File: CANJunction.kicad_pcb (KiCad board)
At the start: 2 copper layers, 46.3 x 22.6 mm, 7 parts, among them J1 Screw_Terminal_01x02, J2 Screw_Terminal_01x06, J3 Screw_Terminal_01x02

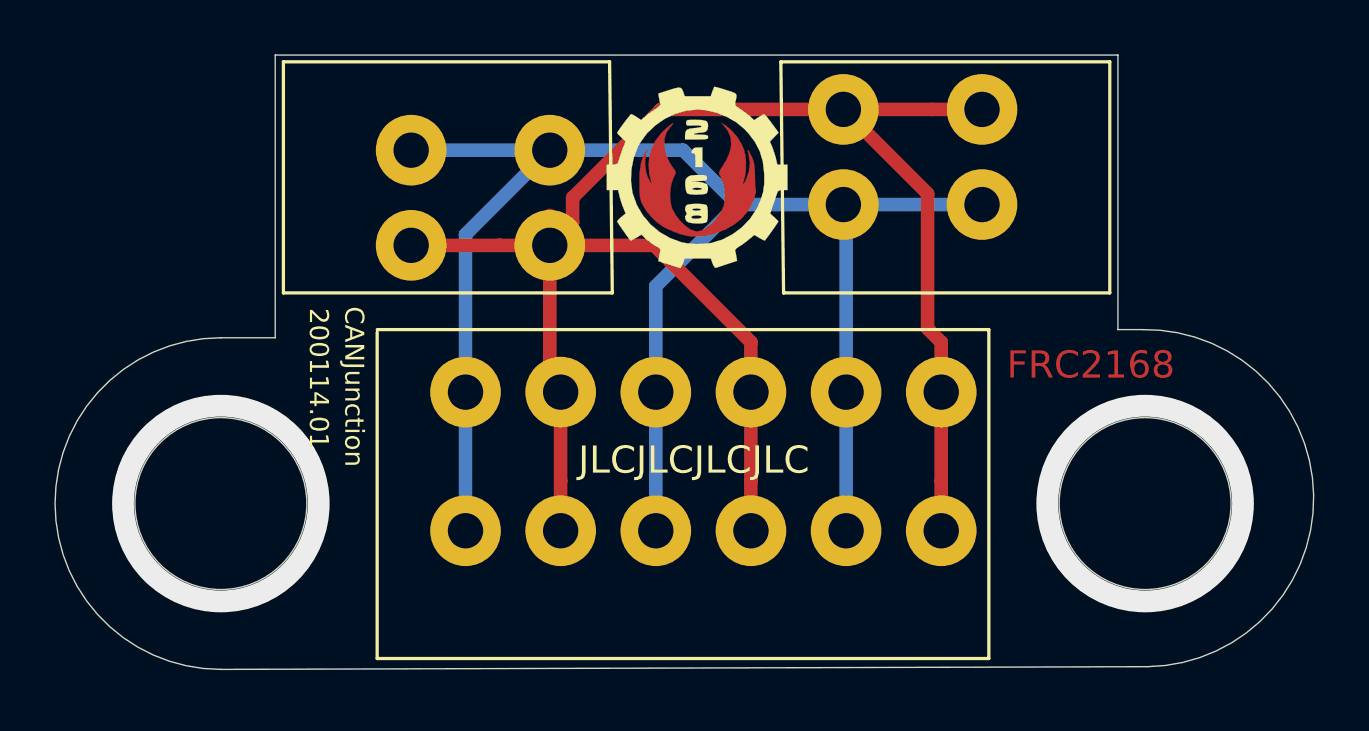
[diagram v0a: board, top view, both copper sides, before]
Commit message: update layout mod hole to fit  3/16” rivet or “10 bolt
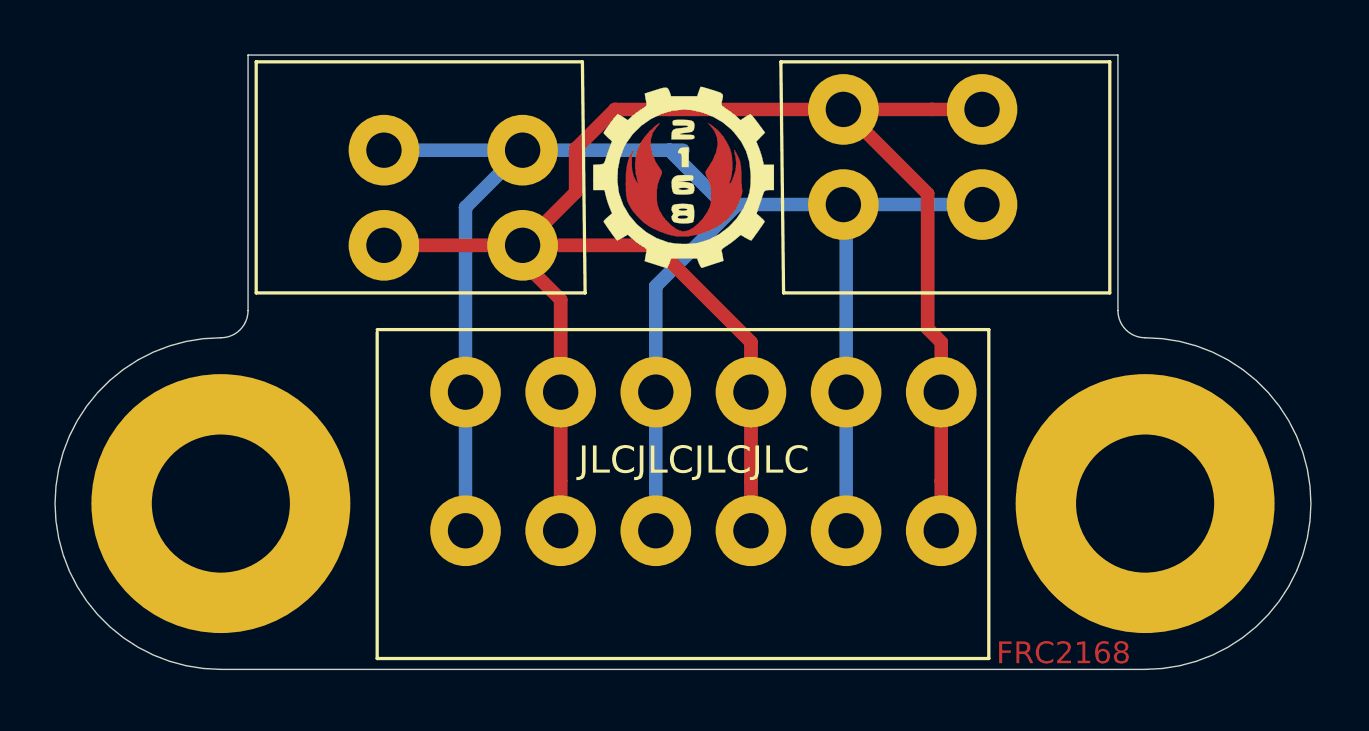
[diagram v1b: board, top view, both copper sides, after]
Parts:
- added H1: MountingHole, _canjunction:mounting_holes, F.Cu at (126.0, 66.0)
- moved J1 1.00 mm to (132.0, 53.0)
- moved G*** 0.50 mm to (143.0, 54.0) (x2)
- moved Wings 0.50 mm to (143.0, 54.0) (x2)
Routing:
- net Net-(J1-Pad2): track 68.2 -> 71.3 mm
- net (no net): vias 2 -> 0
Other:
- board size 46.3 x 22.6 mm -> 46.2 x 22.6 mm
- rule pad_to_mask_clearance: 0.051 -> 0
- board text added: "211209.01"
- board text removed: "200114.01"

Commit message: add direction to fab on where to place order number
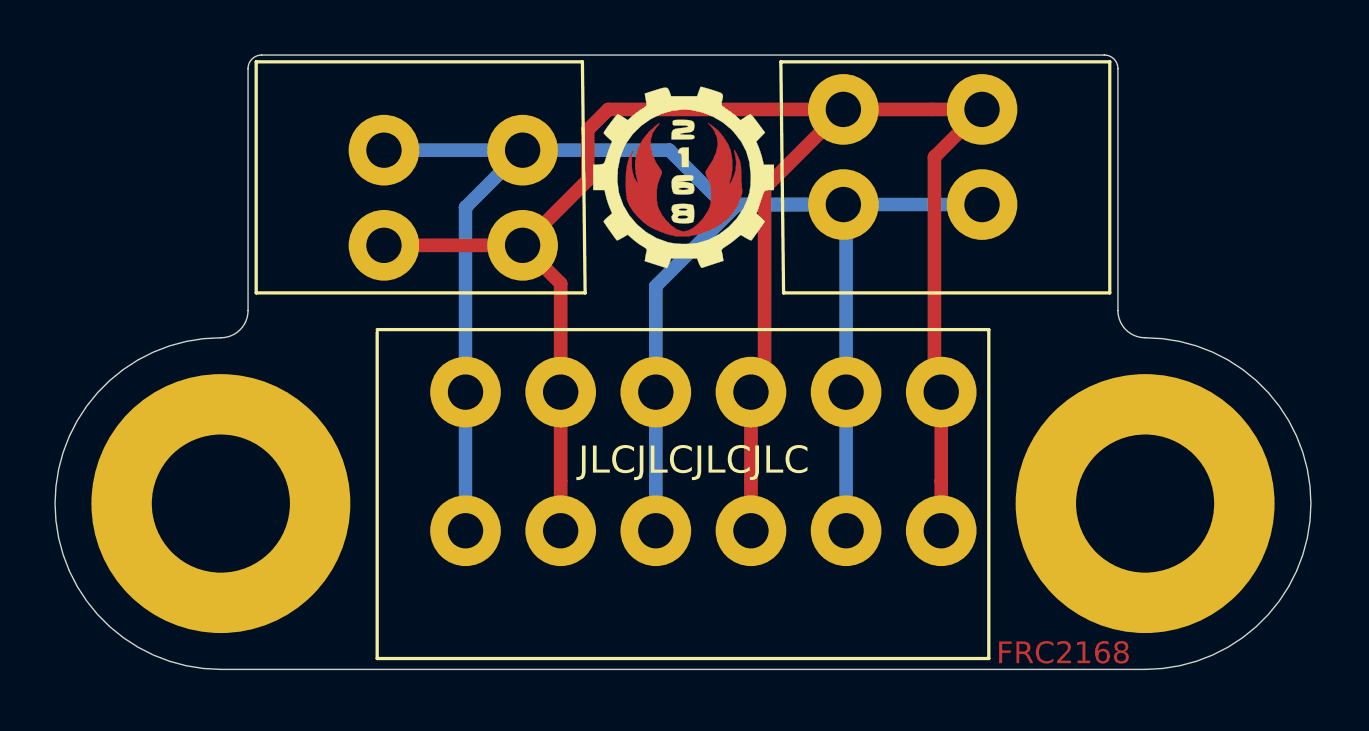
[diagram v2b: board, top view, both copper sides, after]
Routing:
- net Net-(J1-Pad1): track 62.0 -> 66.9 mm
- net Net-(J1-Pad2): track 71.3 -> 70.0 mm
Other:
- outline, holes or cut-outs redrawn
- board text added: "Place Order Number in place of text "JLCJLCJLCJLC" on F.Silk layer"
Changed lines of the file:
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@@
   (general
     (thickness 1.6)
-    (drawings 15)
-    (tracks 40)
+    (drawings 22)
+    (tracks 37)
     (zones 0)
     (modules 8)
@@
     (38 B.Mask user)
     (39 F.Mask user)
-    (40 Dwgs.User user)
-    (41 Cmts.User user)
+    (40 Dwgs.User user hide)
+    (41 Cmts.User user hide)
     (42 Eco1.User user)
     (43 Eco2.User user)
     (44 Edge.Cuts user)
     (45 Margin user)
-    (46 B.CrtYd user)
-    (47 F.CrtYd user)
-    (48 B.Fab user)
+    (46 B.CrtYd user hide)
+    (47 F.CrtYd user hide)
+    (48 B.Fab user hide)
     (49 F.Fab user)
   )
@@
     (pad_to_mask_clearance 0)
     (aux_axis_origin 0 0)
-    (visible_elements 7FFFFFFF)
+    (visible_elements 7FFFFF9F)
     (pcbplotparams
-      (layerselection 0x010fc_ffffffff)
+      (layerselection 0x012fc_ffffffff)
       (usegerberextensions false)
       (usegerberattributes false)
@@
       (effects (font (size 1 1) (thickness 0.15)))
     )
-    (fp_text value MountingHole (at 0 -0.5) (layer F.Fab)
+    (fp_text value MountingHole (at 0 -0.5) (layer F.Fab) hide
       (effects (font (size 1 1) (thickness 0.15)))
     )
@@
     )
   )
+  (gr_line (start 143.75 65.25) (end 143.75 74.75) (layer F.Fab) (width 0.15))
+  (gr_line (start 143 66.5) (end 144.5 66.5) (layer F.Fab) (width 0.15))
+  (gr_line (start 144.5 66.5) (end 143.75 65.25) (layer F.Fab) (width 0.15))
+  (gr_line (start 143.75 65.25) (end 143 66.5) (layer F.Fab) (width 0.15))
+  (gr_text "Place Order Number in place of\ntext \"JLCJLCJLCJLC\" on F.Silk layer" (at 143.75 76.75) (layer F.Fab)
+    (effects (font (size 1 1) (thickness 0.15)))
+  )
+  (gr_arc (start 158.5 50) (end 159 50) (angle -90) (layer Edge.Cuts) (width 0.05))
+  (gr_arc (start 127.5 50) (end 127.5 49.5) (angle -90) (layer Edge.Cuts) (width 0.05))
   (gr_arc (start 126 58.9) (end 126 59.9) (angle -90) (layer Edge.Cuts) (width 0.05))
   (gr_line (start 126 72.1) (end 160 72.1) (layer Edge.Cuts) (width 0.05))
@@
     (effects (font (size 1 1) (thickness 0.15)) (justify mirror))
   )
-  (gr_line (start 127 58.9) (end 127 49.5) (layer Edge.Cuts) (width 0.05))
-  (gr_line (start 159 49.5) (end 159 58.9) (layer Edge.Cuts) (width 0.05))
-  (gr_line (start 127 49.5) (end 159 49.5) (layer Edge.Cuts) (width 0.05))
+  (gr_line (start 127 58.9) (end 127 50) (layer Edge.Cuts) (width 0.05))
+  (gr_line (start 159 50) (end 159 58.9) (layer Edge.Cuts) (width 0.05))
+  (gr_line (start 127.5 49.5) (end 158.5 49.5) (layer Edge.Cuts) (width 0.05))
   (segment (start 148.9 55) (end 145 55) (width 0.5) (layer B.Cu) (net 1))
-  (segment (start 138.1 53) (end 143 53) (width 0.5) (layer B.Cu) (net 1))
-  (segment (start 142.5 53) (end 144.5 55) (width 0.5) (layer B.Cu) (net 1))
   (segment (start 154 55) (end 148.9 55) (width 0.5) (layer B.Cu) (net 1))
   (segment (start 135 61.9) (end 135 67) (width 0.5) (layer B.Cu) (net 1))
@@
   (segment (start 137.1 53) (end 135 55.1) (width 0.5) (layer B.Cu) (net 1))
   (segment (start 137.1 53) (end 132 53) (width 0.5) (layer B.Cu) (net 1))
+  (segment (start 142.5 53) (end 137.1 53) (width 0.5) (layer B.Cu) (net 1))
+  (segment (start 144.5 55) (end 142.5 53) (width 0.5) (layer B.Cu) (net 1))
+  (segment (start 148.9 55) (end 144.5 55) (width 0.5) (layer B.Cu) (net 1))
   (segment (start 152.161523 51.5) (end 148.9 51.5) (width 0.5) (layer F.Cu) (net 2))
   (segment (start 154 51.5) (end 152.161523 51.5) (width 0.5) (layer F.Cu) (net 2))
-  (segment (start 138.1 56.5) (end 136.261523 56.5) (width 0.5) (layer F.Cu) (net 2))
   (segment (start 138.1 61.5) (end 138.5 61.9) (width 0.5) (layer F.Cu) (net 2))
   (segment (start 138.5 65.161523) (end 138.5 61.9) (width 0.5) (layer F.Cu) (net 2))
@@
   (segment (start 152.5 65.161523) (end 152.5 61.9) (width 0.5) (layer F.Cu) (net 2))
   (segment (start 152.5 67) (end 152.5 65.161523) (width 0.5) (layer F.Cu) (net 2))
-  (segment (start 148.9 51.5) (end 152 54.6) (width 0.5) (layer F.Cu) (net 2))
-  (segment (start 152.5 60.061523) (end 152.5 61.9) (width 0.5) (layer F.Cu) (net 2))
-  (segment (start 152 59.561523) (end 152.5 60.061523) (width 0.5) (layer F.Cu) (net 2))
-  (segment (start 152 54.6) (end 152 59.561523) (width 0.5) (layer F.Cu) (net 2))
-  (segment (start 145.5 60.061523) (end 145.5 61.9) (width 0.5) (layer F.Cu) (net 2))
-  (segment (start 138.1 56.5) (end 141.938477 56.5) (width 0.5) (layer F.Cu) (net 2))
-  (segment (start 141.938477 56.5) (end 145.5 60.061523) (width 0.5) (layer F.Cu) (net 2))
-  (segment (start 137.1 56.5) (end 137.1 57.1) (width 0.5) (layer F.Cu) (net 2))
-  (segment (start 138.5 58.5) (end 138.5 61.9) (width 0.5) (layer F.Cu) (net 2))
-  (segment (start 137.1 57.1) (end 138.5 58.5) (width 0.5) (layer F.Cu) (net 2))
   (segment (start 132 56.5) (end 137.1 56.5) (width 0.5) (layer F.Cu) (net 2))
-  (segment (start 139.05 54.55) (end 139.05 52.95) (width 0.5) (layer F.Cu) (net 2))
-  (segment (start 139.05 54.55) (end 137.1 56.5) (width 0.5) (layer F.Cu) (net 2))
-  (segment (start 140.5 51.5) (end 142.5 51.5) (width 0.5) (layer F.Cu) (net 2))
-  (segment (start 139.05 52.95) (end 140.5 51.5) (width 0.5) (layer F.Cu) (net 2))
-  (segment (start 148.9 51.5) (end 142.5 51.5) (width 0.5) (layer F.Cu) (net 2))
+  (segment (start 137.1 56.5) (end 139.5 54.1) (width 0.5) (layer F.Cu) (net 2))
+  (segment (start 139.5 54.1) (end 139.5 52.25) (width 0.5) (layer F.Cu) (net 2))
+  (segment (start 140.25 51.5) (end 148.9 51.5) (width 0.5) (layer F.Cu) (net 2))
+  (segment (start 139.5 52.25) (end 140.25 51.5) (width 0.5) (layer F.Cu) (net 2))
+  (segment (start 138.5 57.9) (end 137.1 56.5) (width 0.5) (layer F.Cu) (net 2))
+  (segment (start 138.5 61.9) (end 138.5 57.9) (width 0.5) (layer F.Cu) (net 2))
+  (segment (start 148.9 51.5) (end 146 54.4) (width 0.5) (layer F.Cu) (net 2))
+  (segment (start 146 61.4) (end 145.5 61.9) (width 0.5) (layer F.Cu) (net 2))
+  (segment (start 146 54.4) (end 146 61.4) (width 0.5) (layer F.Cu) (net 2))
+  (segment (start 152.249999 61.649999) (end 152.5 61.9) (width 0.5) (layer F.Cu) (net 2))
+  (segment (start 152.249999 53.250001) (end 152.249999 61.649999) (width 0.5) (layer F.Cu) (net 2))
+  (segment (start 154 51.5) (end 152.249999 53.250001) (width 0.5) (layer F.Cu) (net 2))
 )
